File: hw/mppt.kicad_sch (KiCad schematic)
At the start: 10 parts

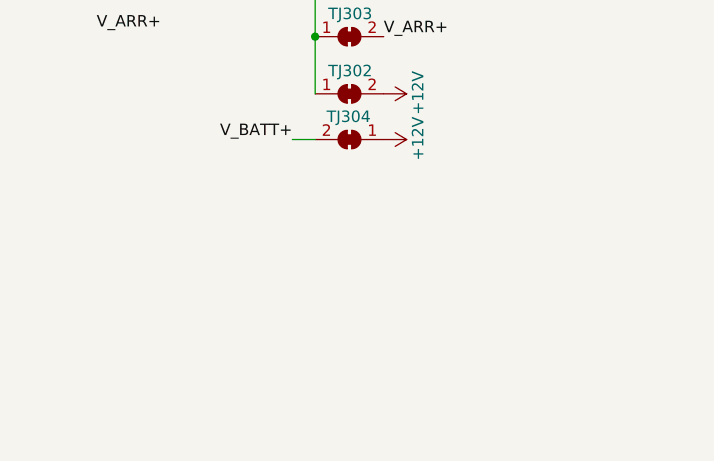
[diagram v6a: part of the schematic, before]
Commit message: changed low-speed test points to through-hole standoffs, created a thermal sink area for high-side fet on B.Cu, and changed some thermal resistors to larger 1225 package where available due to lower cost and better thermal resistance
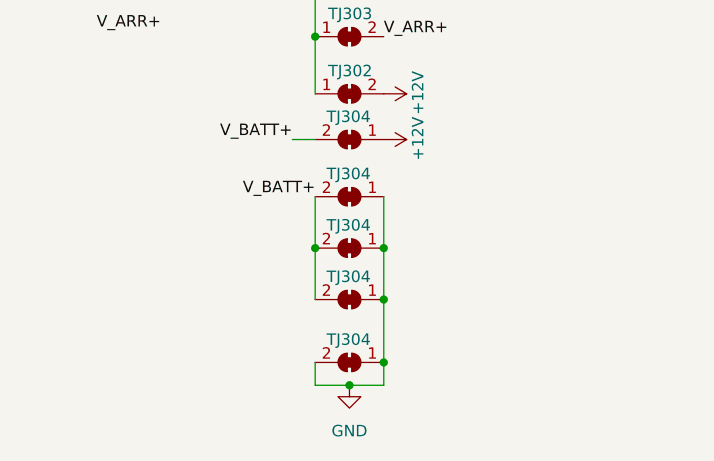
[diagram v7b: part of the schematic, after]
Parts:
- added TJ304 (x3): Thermal Jumper, mppt:1225_SMD, symbol Jumper:SolderJumper_2_Bridged
- added TJ304: Thermal Jumper, Resistor_SMD:R_0805_2012Metric, symbol Jumper:SolderJumper_2_Bridged
- TJ303: footprint Resistor_SMD:R_0805_2012Metric -> mppt:1225_SMD; Mfr PN QB0805B40WYT -> THJP2512ABT1
- TJ303: footprint Resistor_SMD:R_0805_2012Metric -> mppt:1225_SMD
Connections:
- net V_BATT+: now also TJ304.2 (B), TJ304.2 (B), TJ304.2 (B)
- new net GND: TJ304.1 (A), TJ304.1 (A), TJ304.1 (A), TJ304.1 (A), TJ304.2 (B)
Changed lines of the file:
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@@
     (comment 3 "Matthew Yu")
   )
+  (junction (at 68.58 174.625) (diameter 0) (color 0 0 0 0)
+  )
+  (junction (at 64.77 184.15) (diameter 0) (color 0 0 0 0)
+  )
   (junction (at 60.96 139.7) (diameter 0) (color 0 0 0 0)
   )
@@
   (junction (at 60.96 145.415) (diameter 0) (color 0 0 0 0)
   )
+  (junction (at 68.58 168.91) (diameter 0) (color 0 0 0 0)
+  )
   (junction (at 60.96 127) (diameter 0) (color 0 0 0 0)
   )
+  (junction (at 60.96 168.91) (diameter 0) (color 0 0 0 0)
+  )
+  (junction (at 68.58 181.61) (diameter 0) (color 0 0 0 0)
+  )
+  (wire (pts (xy 60.96 184.15) (xy 64.77 184.15))
+    (stroke (width 0) (type default))
+  )
   (wire (pts (xy 60.96 139.7) (xy 60.96 145.415))
     (stroke (width 0) (type default))
@@
     (stroke (width 0) (type default))
   )
+  (wire (pts (xy 60.96 163.195) (xy 60.96 168.91))
+    (stroke (width 0) (type default))
+  )
   (wire (pts (xy 60.96 127) (xy 60.96 133.35))
     (stroke (width 0) (type default))
   )
+  (wire (pts (xy 68.58 174.625) (xy 68.58 181.61))
+    (stroke (width 0) (type default))
+  )
   (wire (pts (xy 29.21 40.64) (xy 29.21 73.66))
     (stroke (width 0) (type default))
@@
     (stroke (width 0) (type default))
   )
+  (wire (pts (xy 68.58 168.91) (xy 68.58 174.625))
+    (stroke (width 0) (type default))
+  )
   (wire (pts (xy 80.01 54.61) (xy 80.01 69.85))
     (stroke (width 0) (type default))
   )
+  (wire (pts (xy 60.96 168.91) (xy 60.96 174.625))
+    (stroke (width 0) (type default))
+  )
+  (wire (pts (xy 60.96 181.61) (xy 60.96 184.15))
+    (stroke (width 0) (type default))
+  )
   (wire (pts (xy 72.39 83.82) (xy 83.82 83.82))
     (stroke (width 0) (type default))
@@
     (stroke (width 0) (type default))
   )
+  (wire (pts (xy 64.77 184.15) (xy 68.58 184.15))
+    (stroke (width 0) (type default))
+  )
   (wire (pts (xy 125.73 57.15) (xy 125.73 69.85))
     (stroke (width 0) (type default))
@@
     (stroke (width 0) (type default))
   )
+  (wire (pts (xy 68.58 163.195) (xy 68.58 168.91))
+    (stroke (width 0) (type default))
+  )
   (wire (pts (xy 72.39 76.2) (xy 83.82 76.2))
     (stroke (width 0) (type default))
@@
   )
   (wire (pts (xy 72.39 40.64) (xy 83.82 40.64))
+    (stroke (width 0) (type default))
+  )
+  (wire (pts (xy 68.58 181.61) (xy 68.58 184.15))
     (stroke (width 0) (type default))
   )
@@
     (effects (font (size 1.27 1.27)) (justify left bottom))
   )
+  (label "V_BATT+" (at 60.96 163.195 180) (fields_autoplaced)
+    (effects (font (size 1.27 1.27)) (justify right bottom))
+  )
   (label "V_BATT+" (at 68.58 139.7 0) (fields_autoplaced)
     (effects (font (size 1.27 1.27)) (justify left bottom))
@@
       (effects (font (size 1.27 1.27)) (justify right) hide)
     )
-    (property "Footprint" "Resistor_SMD:R_0805_2012Metric" (at 64.77 139.7 0)
+    (property "Footprint" "mppt:1225_SMD" (at 64.77 139.7 0)
       (effects (font (size 1.27 1.27)) hide)
     )
@@
       (effects (font (size 1.27 1.27)) hide)
     )
-    (property "Mfr PN" "QB0805B40WYT" (at 64.77 139.7 0)
+    (property "Mfr PN" "THJP2512ABT1" (at 64.77 139.7 0)
       (effects (font (size 1.27 1.27)) hide)
     )
@@
         (path "/06fd3a42-664d-41bc-bf0f-b5ee0ddcc902"
           (reference "TJ101") (unit 1)
+        )
+      )
+    )
+  )
+  (symbol (lib_id "Jumper:SolderJumper_2_Bridged") (at 64.77 181.61 180) (unit 1)
+    (in_bom yes) (on_board yes) (dnp no)
+    (property "Reference" "TJ304" (at 62.23 179.07 0)
+      (effects (font (size 1.27 1.27)) (justify right))
+    )
+    (property "Value" "Thermal Jumper" (at 58.42 179.07 0)
+      (effects (font (size 1.27 1.27)) (justify right) hide)
+    )
+    (property "Footprint" "mppt:1225_SMD" (at 64.77 181.61 0)
+      (effects (font (size 1.27 1.27)) hide)
+    )
+    (property "Datasheet" "~" (at 64.77 181.61 0)
+      (effects (font (size 1.27 1.27)) hide)
+    )
+    (property "Mfr PN" "THJP2512ABT1" (at 64.77 181.61 0)
+      (effects (font (size 1.27 1.27)) hide)
+    )
+    (pin "1")
+    (pin "2")
+    (instances
+      (project "mppt"
+        (path "/06fd3a42-664d-41bc-bf0f-b5ee0ddcc902/9cd55a57-0ec8-481d-b571-b5fdbe353ce7"
+          (reference "TJ304") (unit 1)
+        )
+        (path "/06fd3a42-664d-41bc-bf0f-b5ee0ddcc902"
+          (reference "TJ108") (unit 1)
         )
       )
@@
     )
   )
+  (symbol (lib_id "Jumper:SolderJumper_2_Bridged") (at 64.77 174.625 180) (unit 1)
+    (in_bom yes) (on_board yes) (dnp no)
+    (property "Reference" "TJ304" (at 62.23 172.085 0)
+      (effects (font (size 1.27 1.27)) (justify right))
+    )
+    (property "Value" "Thermal Jumper" (at 58.42 172.085 0)
+      (effects (font (size 1.27 1.27)) (justify right) hide)
+    )
+    (property "Footprint" "mppt:1225_SMD" (at 64.77 174.625 0)
+      (effects (font (size 1.27 1.27)) hide)
+    )
+    (property "Datasheet" "~" (at 64.77 174.625 0)
+      (effects (font (size 1.27 1.27)) hide)
+    )
+    (property "Mfr PN" "THJP2512ABT1" (at 64.77 174.625 0)
+      (effects (font (size 1.27 1.27)) hide)
+    )
+    (pin "1")
+    (pin "2")
+    (instances
+      (project "mppt"
+        (path "/06fd3a42-664d-41bc-bf0f-b5ee0ddcc902/9cd55a57-0ec8-481d-b571-b5fdbe353ce7"
+          (reference "TJ304") (unit 1)
+        )
+        (path "/06fd3a42-664d-41bc-bf0f-b5ee0ddcc902"
+          (reference "TJ110") (unit 1)
+        )
+      )
+    )
+  )
   (symbol (lib_id "Jumper:SolderJumper_2_Bridged") (at 64.77 145.415 0) (unit 1)
     (in_bom yes) (on_board yes) (dnp no)
@@
       (effects (font (size 1.27 1.27)) (justify right) hide)
     )
-    (property "Footprint" "Resistor_SMD:R_0805_2012Metric" (at 64.77 133.35 0)
+    (property "Footprint" "mppt:1225_SMD" (at 64.77 133.35 0)
       (effects (font (size 1.27 1.27)) hide)
     )
@@
         (path "/06fd3a42-664d-41bc-bf0f-b5ee0ddcc902"
           (reference "TJ102") (unit 1)
+        )
+      )
+    )
+  )
+  (symbol (lib_id "Jumper:SolderJumper_2_Bridged") (at 64.77 168.91 180) (unit 1)
+    (in_bom yes) (on_board yes) (dnp no)
+    (property "Reference" "TJ304" (at 62.23 166.37 0)
+      (effects (font (size 1.27 1.27)) (justify right))
+    )
+    (property "Value" "Thermal Jumper" (at 58.42 166.37 0)
+      (effects (font (size 1.27 1.27)) (justify right) hide)
+    )
+    (property "Footprint" "mppt:1225_SMD" (at 64.77 168.91 0)
+      (effects (font (size 1.27 1.27)) hide)
+    )
+    (property "Datasheet" "~" (at 64.77 168.91 0)
+      (effects (font (size 1.27 1.27)) hide)
+    )
+    (property "Mfr PN" "THJP2512ABT1" (at 64.77 168.91 0)
+      (effects (font (size 1.27 1.27)) hide)
+    )
+    (pin "1")
+    (pin "2")
+    (instances
+      (project "mppt"
+        (path "/06fd3a42-664d-41bc-bf0f-b5ee0ddcc902/9cd55a57-0ec8-481d-b571-b5fdbe353ce7"
+          (reference "TJ304") (unit 1)
+        )
+        (path "/06fd3a42-664d-41bc-bf0f-b5ee0ddcc902"
+          (reference "TJ109") (unit 1)
         )
       )
@@
     )
   )
+  (symbol (lib_id "power:GND") (at 64.77 184.15 0) (unit 1)
+    (in_bom yes) (on_board yes) (dnp no) (fields_autoplaced)
+    (property "Reference" "#PWR01" (at 64.77 190.5 0)
+      (effects (font (size 1.27 1.27)) hide)
+    )
+    (property "Value" "GND" (at 64.77 189.23 0)
+      (effects (font (size 1.27 1.27)))
+    )
+    (property "Footprint" "" (at 64.77 184.15 0)
+      (effects (font (size 1.27 1.27)) hide)
+    )
+    (property "Datasheet" "" (at 64.77 184.15 0)
+      (effects (font (size 1.27 1.27)) hide)
+    )
+    (pin "1")
+    (instances
+      (project "mppt"
+        (path "/06fd3a42-664d-41bc-bf0f-b5ee0ddcc902"
+          (reference "#PWR01") (unit 1)
+        )
+      )
+    )
+  )
   (symbol (lib_id "Jumper:SolderJumper_2_Bridged") (at 64.77 151.765 0) (unit 1)
     (in_bom yes) (on_board yes) (dnp no)
@@
         )
       )
+    )
+  )
+  (symbol (lib_id "Jumper:SolderJumper_2_Bridged") (at 64.77 163.195 180) (unit 1)
+    (in_bom yes) (on_board yes) (dnp no)
+    (property "Reference" "TJ304" (at 62.23 160.655 0)
+      (effects (font (size 1.27 1.27)) (justify right))
+    )
+    (property "Value" "Thermal Jumper" (at 58.42 160.655 0)
+      (effects (font (size 1.27 1.27)) (justify right) hide)
+    )
+    (property "Footprint" "Resistor_SMD:R_0805_2012Metric" (at 64.77 163.195 0)
+      (effects (font (size 1.27 1.27)) hide)
+    )
+    (property "Datasheet" "~" (at 64.77 163.195 0)
+      (effects (font (size 1.27 1.27)) hide)
+    )
+    (property "Mfr PN" "QB0805B40WYT" (at 64.77 163.195 0)
+      (effects (font (size 1.27 1.27)) hide)
+    )
+    (pin "1")
+    (pin "2")
+    (instances
+      (project "mppt"
+        (path "/06fd3a42-664d-41bc-bf0f-b5ee0ddcc902/9cd55a57-0ec8-481d-b571-b5fdbe353ce7"
+          (reference "TJ304") (unit 1)
+        )
+        (path "/06fd3a42-664d-41bc-bf0f-b5ee0ddcc902"
+          (reference "TJ107") (unit 1)
+        )
+      )

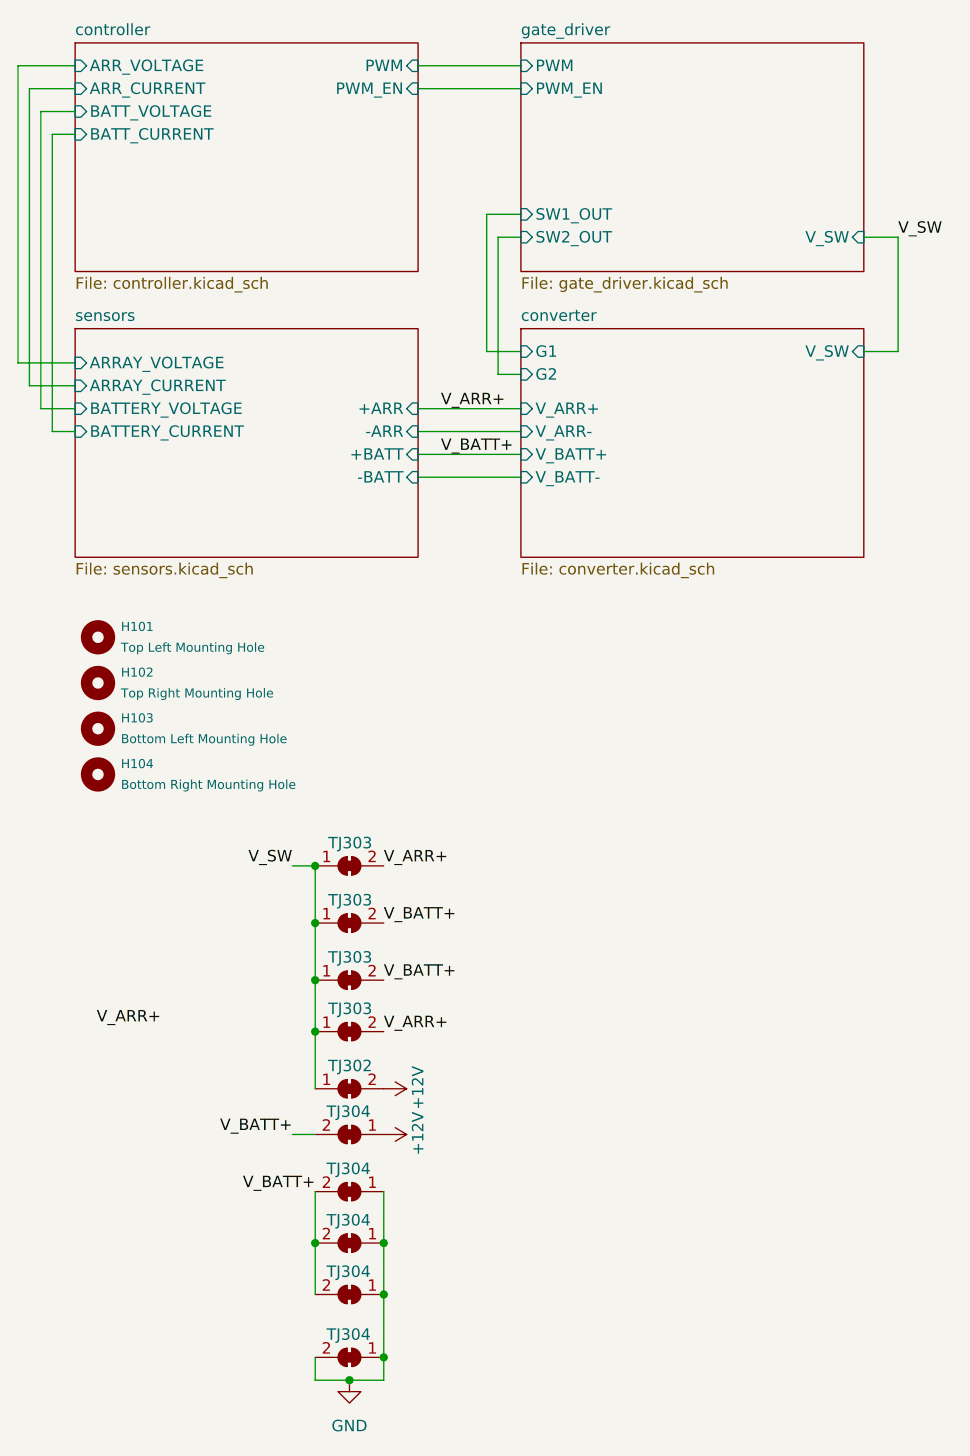
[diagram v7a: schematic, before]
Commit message: rebuild schematic, passes ERC, bom completed
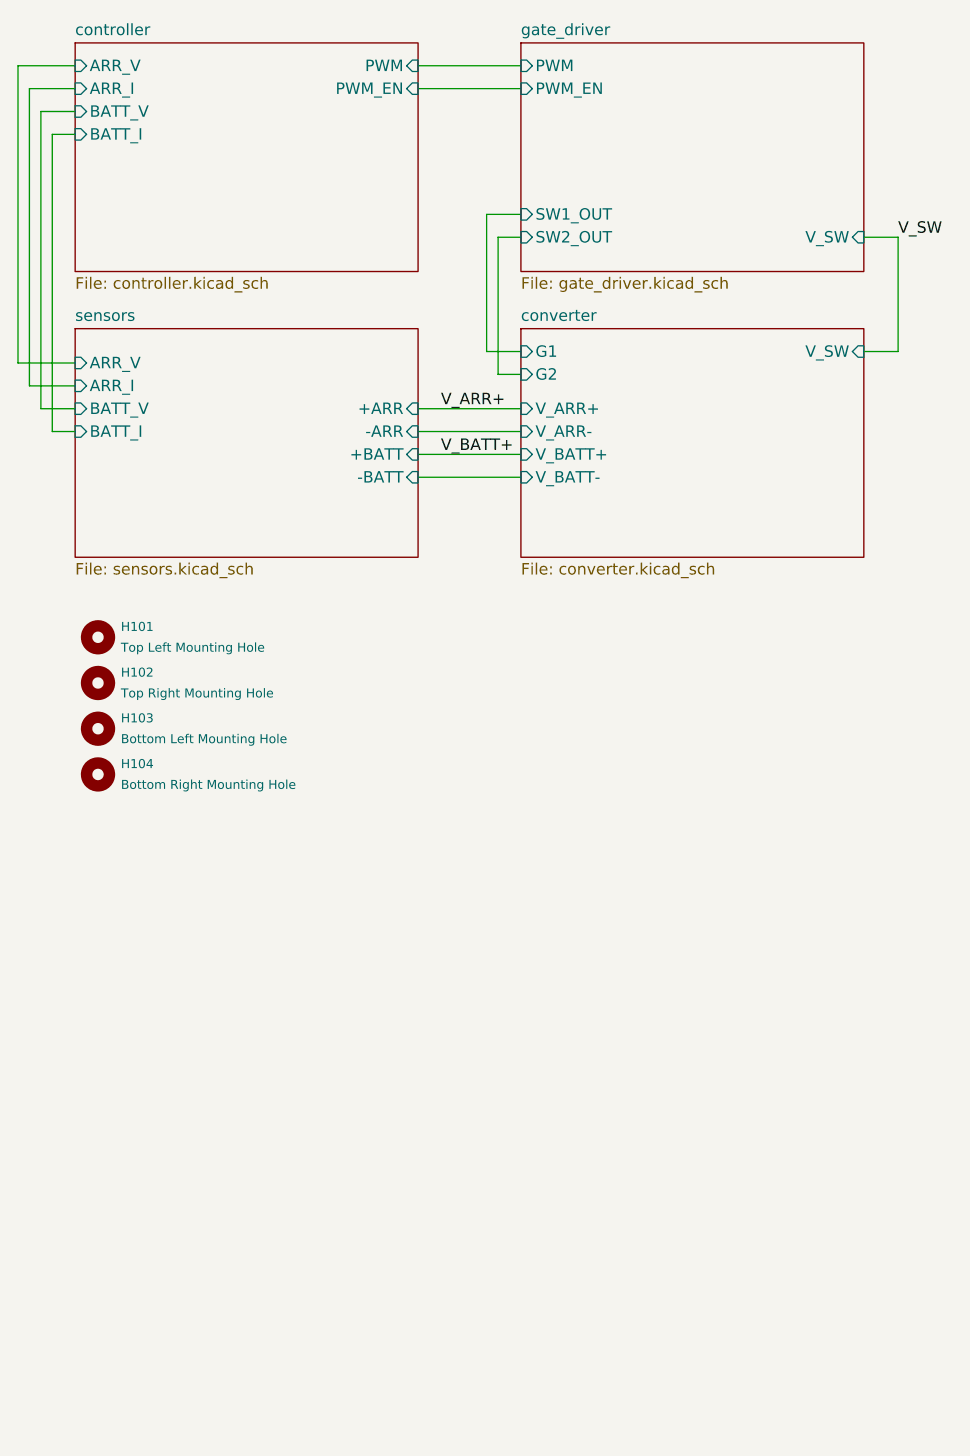
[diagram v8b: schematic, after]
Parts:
- removed TJ302, TJ303 (x2), TJ304 (x2): Thermal Jumper, Resistor_SMD:R_0805_2012Metric, symbol Jumper:SolderJumper_2_Bridged
- removed TJ303 (x2), TJ304 (x3): Thermal Jumper, mppt:1225_SMD, symbol Jumper:SolderJumper_2_Bridged
- H101, H102, H103, H104: footprint MountingHole:MountingHole_2.2mm_M2 -> MountingHole:MountingHole_3.5mm
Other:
- sheet controller ports: added ARR_I, ARR_V, BATT_I, BATT_V; removed ARR_CURRENT, ARR_VOLTAGE, BATT_CURRENT, BATT_VOLTAGE
- sheet sensors ports: added ARR_I, ARR_V, BATT_I, BATT_V; removed ARRAY_CURRENT, ARRAY_VOLTAGE, BATTERY_CURRENT, BATTERY_VOLTAGE
